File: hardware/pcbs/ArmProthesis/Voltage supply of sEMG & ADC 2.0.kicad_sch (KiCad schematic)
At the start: 13 parts, among them U1 TLE2426CD, U2 LT1963AEQ

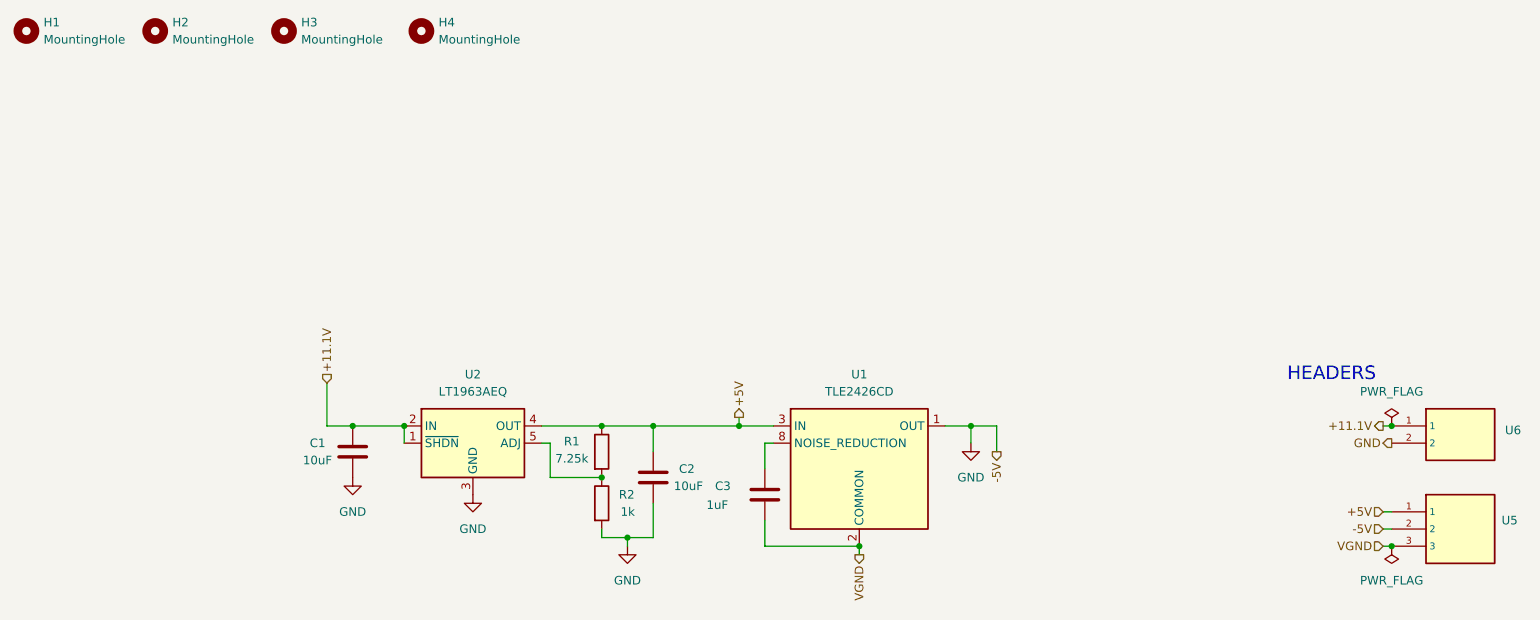
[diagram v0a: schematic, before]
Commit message: new LDO with a proper rail splitter
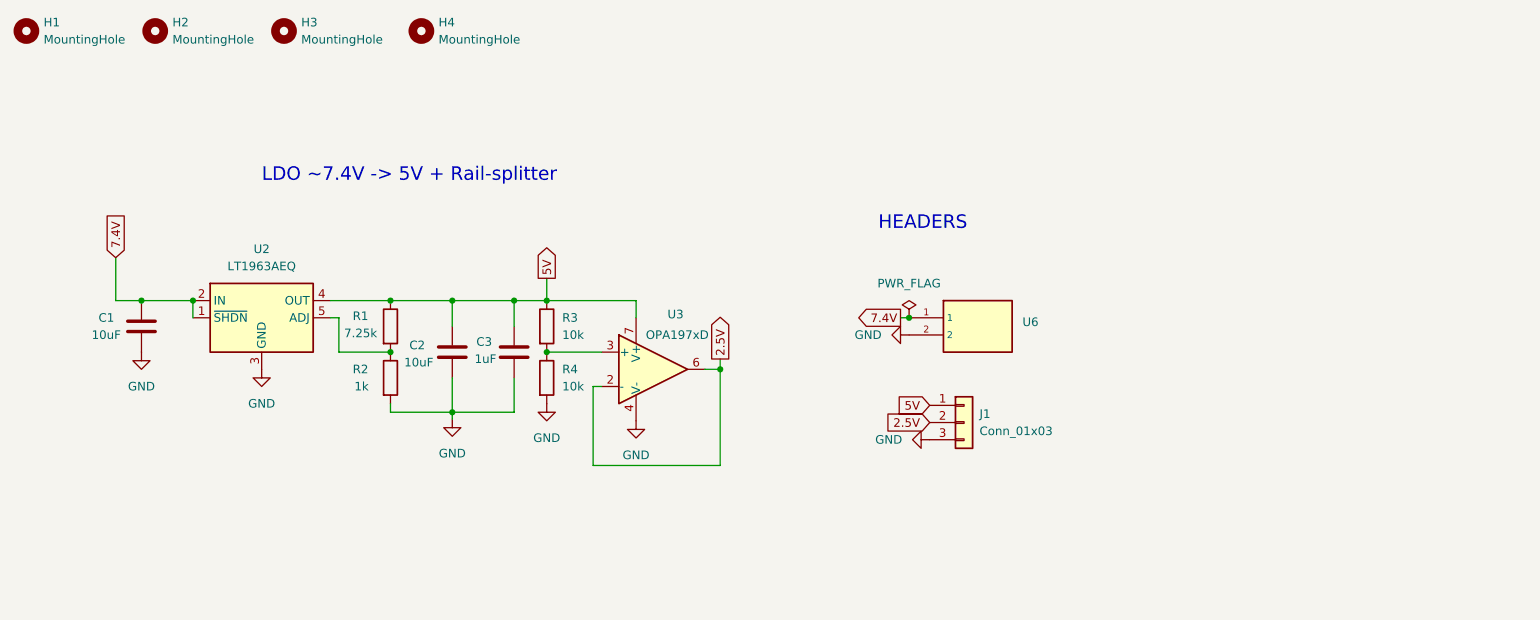
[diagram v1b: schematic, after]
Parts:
- removed U1: TLE2426CD, Package_SO:SOIC-8_3.9x4.9mm_P1.27mm, symbol Reference_Voltage:TLE2426xD
- removed U5: ~, Connector_JST:JST_GH_SM03B-GHS-TB_1x03-1MP_P1.25mm_Horizontal, symbol headers:H_3
- added J1: Conn_01x03, Connector_JST:JST_GH_SM03B-GHS-TB_1x03-1MP_P1.25mm_Horizontal, symbol Connector_Generic:Conn_01x03
- added R3, R4: 10k, Resistor_SMD:R_0402_1005Metric, symbol Device:R
- added U3: OPA197xD, Package_SO:SOIC-8_3.9x4.9mm_P1.27mm, symbol Amplifier_Operational:OPA197xD
- C3: LCSC C86020 -> C16194907
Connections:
- net +5V is gone; now on net 5V: C2.1, R1.1, U2.4 (OUT)
- net VGND is gone; now on net GND: C3.2
- net GND: now also J1.3 (Pin_3), R4.2, U3.4 (V-)
- net 5V: now reaches C3.1
- net 5V: now also J1.1 (Pin_1), R3.1, U3.7 (V+)
- net +11.1V renamed 7.4V
- new net: R3.2, R4.1, U3.3 (+)
- new net 2.5V: J1.2 (Pin_2), U3.2 (-), U3.6
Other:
- note added: "LDO ~7.4V -> 5V + Rail-splitter"
- moved on the sheet: C1, C2, R1, R2, U2, U6

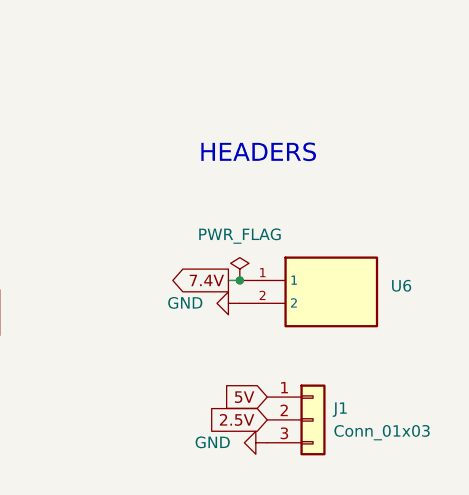
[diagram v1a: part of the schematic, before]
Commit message: Fixed EMG sensors active band pass filter
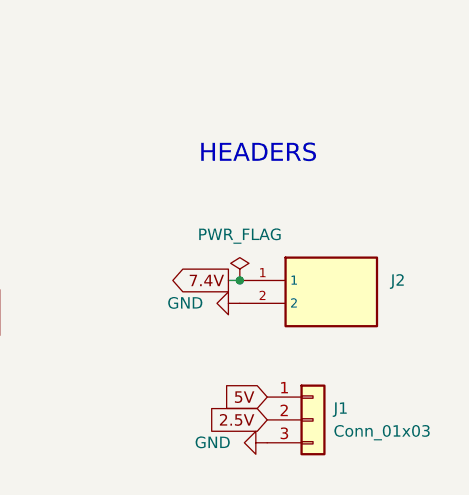
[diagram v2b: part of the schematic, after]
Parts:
- renumbered U6 to J2
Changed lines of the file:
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@@
 		(dnp no)
 		(fields_autoplaced yes)
-		(property "Reference" "U6"
-			(at 177.8 70.9929 0)
+		(property "Reference" "J2"
+			(at 177.8 70.3579 0)
 			(effects
 				(font
@@
 		)
 		(property "Value" "~"
-			(at 177.8 72.898 0)
+			(at 177.8 72.8979 0)
 			(effects
 				(font
@@
 			(project ""
 				(path "/2b971b82-04c2-44b8-8a4b-c54191e7bf3c"
-					(reference "U6")
+					(reference "J2")
 					(unit 1)
 				)

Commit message: Ordered versions
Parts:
- added J3: Conn_01x02, Connector_JST:JST_GH_SM02B-GHS-TB_1x02-1MP_P1.25mm_Horizontal, symbol headers:H_2
- C1, C2: LCSC C16194907 -> C92341
- C3: LCSC C16194907 -> C15849
- J1: LCSC (none) -> C514175
- J2: value ~ -> Conn_01x02
- R1: value 7.25k -> 12.1k; LCSC C25980 -> C22864
- R2: value 1k -> 3.9k; LCSC C21190 -> C114616
- R3, R4: LCSC (none) -> C25744
- U3: LCSC (none) -> C1347124
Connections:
- net 5V: now also J3.2
- net GND: now also J3.1
